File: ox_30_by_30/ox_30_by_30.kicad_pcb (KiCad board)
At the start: 2 copper layers, 30 x 30 mm, 22 parts, among them J1 PIX1, J10 R_CONN, J11 PIX1, J12 PIX2, J13 PIX3, J14 BOT_TCE, J16 PIX4, J17 PIX5, J18 PIX6, J19 TCE4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

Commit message: purge output files
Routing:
- added copper zone on B.Cu, net (none)
- added copper zone on F.Cu, net (none)
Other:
- board text added: "de7ba9e"
- board text removed: "45f1e60"
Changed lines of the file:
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@@
   )
   (setup
-    (last_trace_width 1)
+    (last_trace_width 0.25)
     (user_trace_width 1)
     (trace_clearance 0.2)
-    (zone_clearance 0.508)
+    (zone_clearance 0.2)
     (zone_45_only no)
     (trace_min 0.2)
@@
   (gr_arc (start -8 10) (end -10 10) (angle -90) (layer Edge.Cuts) (width 0.05))
   (gr_arc (start -8 -10) (end -8 -12) (angle -90) (layer Edge.Cuts) (width 0.05))
-  (gr_text 45f1e60 (at 11.5 14) (layer B.SilkS)
+  (gr_text de7ba9e (at 11.5 14) (layer B.SilkS)
     (effects (font (size 1 1) (thickness 0.15)) (justify mirror))
   )
-  (gr_text 45f1e60 (at 11.5 14) (layer F.SilkS)
+  (gr_text de7ba9e (at 11.5 14) (layer F.SilkS)
     (effects (font (size 1 1) (thickness 0.15)))
   )
@@
   (segment (start -12.16 11) (end -11.75 11.41) (width 1) (layer F.Cu) (net 20))
   (segment (start -14 11) (end -12.16 11) (width 1) (layer F.Cu) (net 20))
+  (zone (net 0) (net_name "") (layer F.Cu) (hatch edge 0.508)
+    (connect_pads (clearance 0.2))
+    (min_thickness 0.1)
+    (fill yes (arc_segments 32) (thermal_gap 0.508) (thermal_bridge_width 0.508))
+    (polygon
+      (pts
+        (xy 14.5 14.5) (xy -14.5 14.5) (xy -14.5 -14.5) (xy 14.5 -14.5)
+      )
+    )
+  )
+  (zone (net 0) (net_name "") (layer B.Cu) (hatch edge 0.508)
+    (connect_pads (clearance 0.2))
+    (min_thickness 0.1)
+    (fill yes (arc_segments 32) (thermal_gap 0.508) (thermal_bridge_width 0.508))
+    (polygon
+      (pts
+        (xy 14.5 14.5) (xy -14.5 14.5) (xy -14.5 -14.5) (xy 14.5 -14.5)
+      )
+    )
+  )
 )

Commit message: update silk
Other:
- board text added: "c0adfdf"
- board text removed: "de7ba9e"
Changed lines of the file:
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@@
   (gr_arc (start -8 10) (end -10 10) (angle -90) (layer Edge.Cuts) (width 0.05))
   (gr_arc (start -8 -10) (end -8 -12) (angle -90) (layer Edge.Cuts) (width 0.05))
-  (gr_text de7ba9e (at 11.5 14) (layer B.SilkS)
+  (gr_text c0adfdf (at 11.5 14) (layer B.SilkS)
     (effects (font (size 1 1) (thickness 0.15)) (justify mirror))
   )
-  (gr_text de7ba9e (at 11.5 14) (layer F.SilkS)
+  (gr_text c0adfdf (at 11.5 14) (layer F.SilkS)
     (effects (font (size 1 1) (thickness 0.15)))
   )

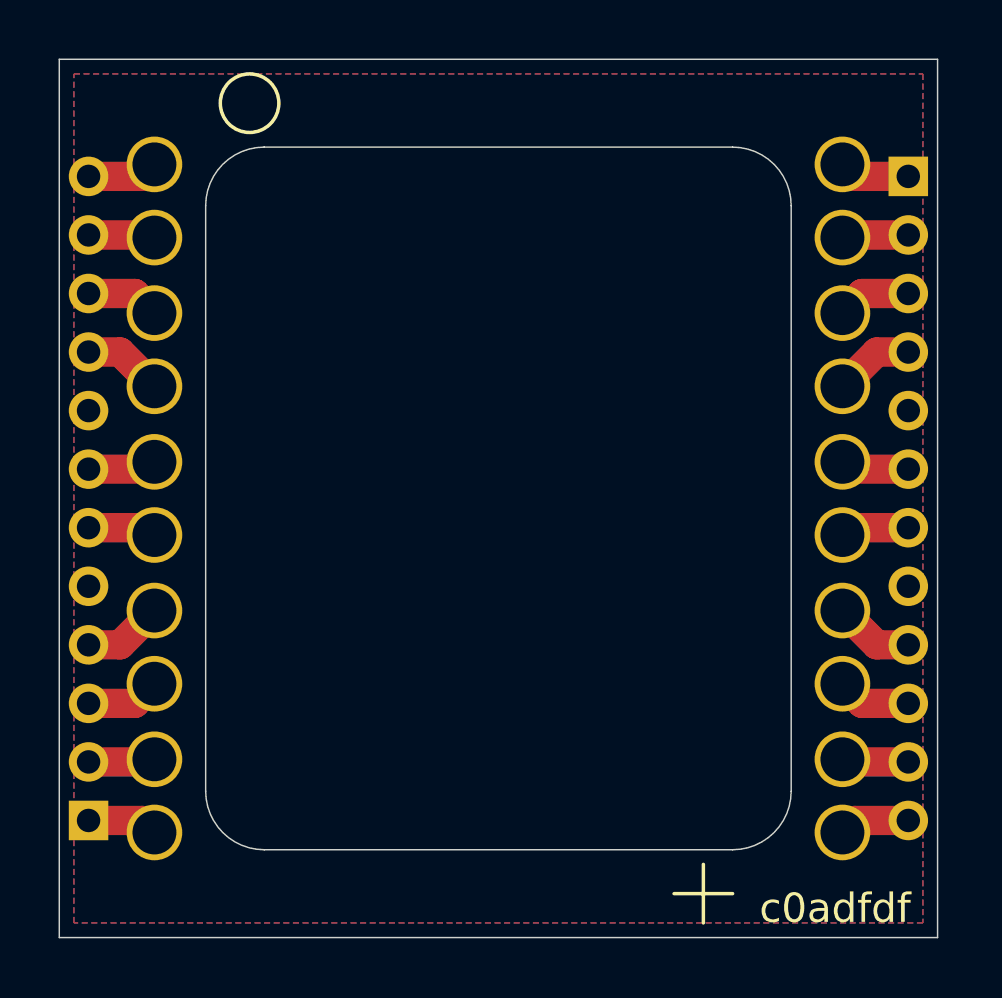
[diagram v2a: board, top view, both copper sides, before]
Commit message: lim crossbar pcb done
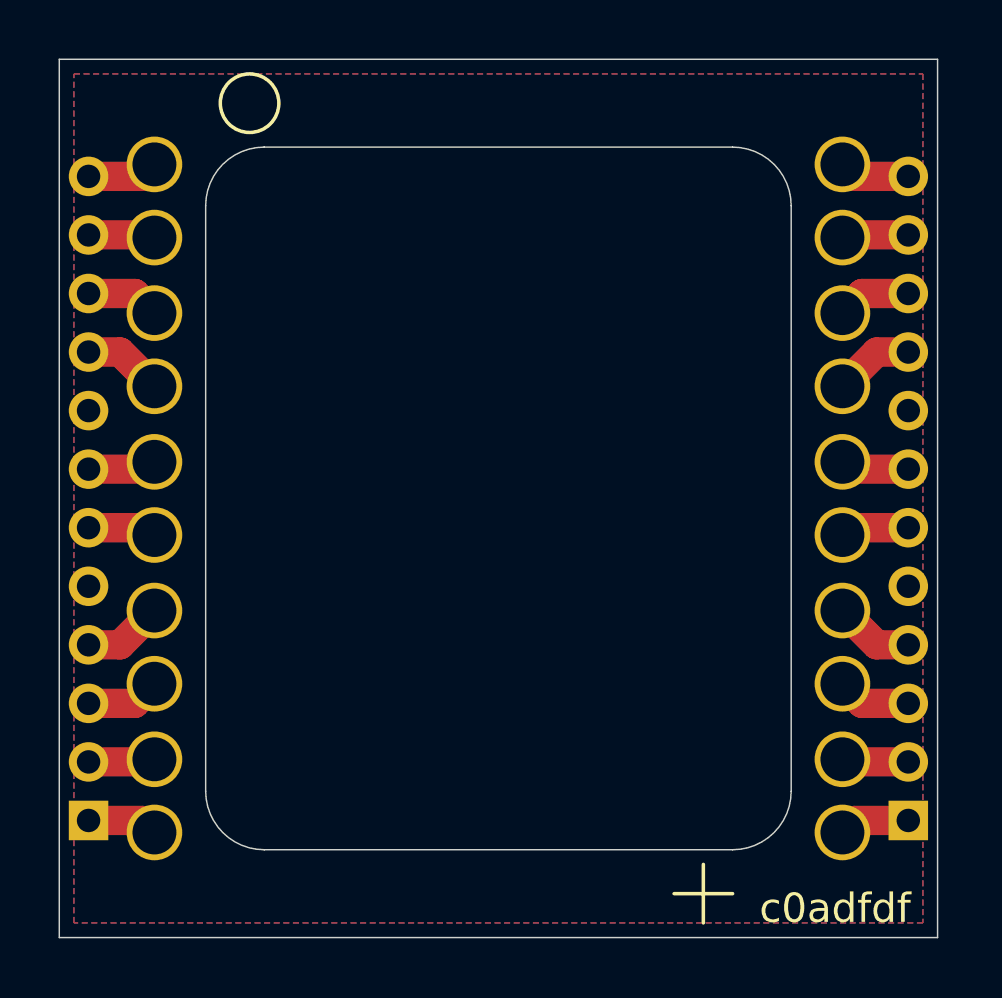
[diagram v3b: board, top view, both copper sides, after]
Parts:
- moved J10 22.0 mm to (14.0, 11.0), turned to 0 degrees
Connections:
- J10 pad 10: Net-(J1-Pad1) -> Net-(J10-Pad10)
- J10 pad 3: Net-(J10-Pad3) -> Net-(J1-Pad1)
- J11 pad 1: Net-(J10-Pad9) -> Net-(J10-Pad4)
- J13 pad 1: Net-(J10-Pad6) -> Net-(J10-Pad7)
- J14 pad 1: Net-(J10-Pad11) -> Net-(J10-Pad2)
- J17 pad 1: Net-(J10-Pad4) -> Net-(J10-Pad9)
- J23 pad 1: Net-(J10-Pad1) -> Net-(J10-Pad12)
- J24 pad 1: Net-(J10-Pad2) -> Net-(J10-Pad11)
- J3 pad 1: Net-(J10-Pad7) -> Net-(J10-Pad6)
- J5 pad 1: Net-(J10-Pad3) -> Net-(J10-Pad10)
- J9 pad 1: Net-(J10-Pad12) -> Net-(J10-Pad1)
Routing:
- net Net-(J10-Pad3): track 2.53 -> 0.00 mm
- net Net-(J10-Pad10): track 0.00 -> 2.53 mm

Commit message: update spring pin hole size and improve crossbar routing
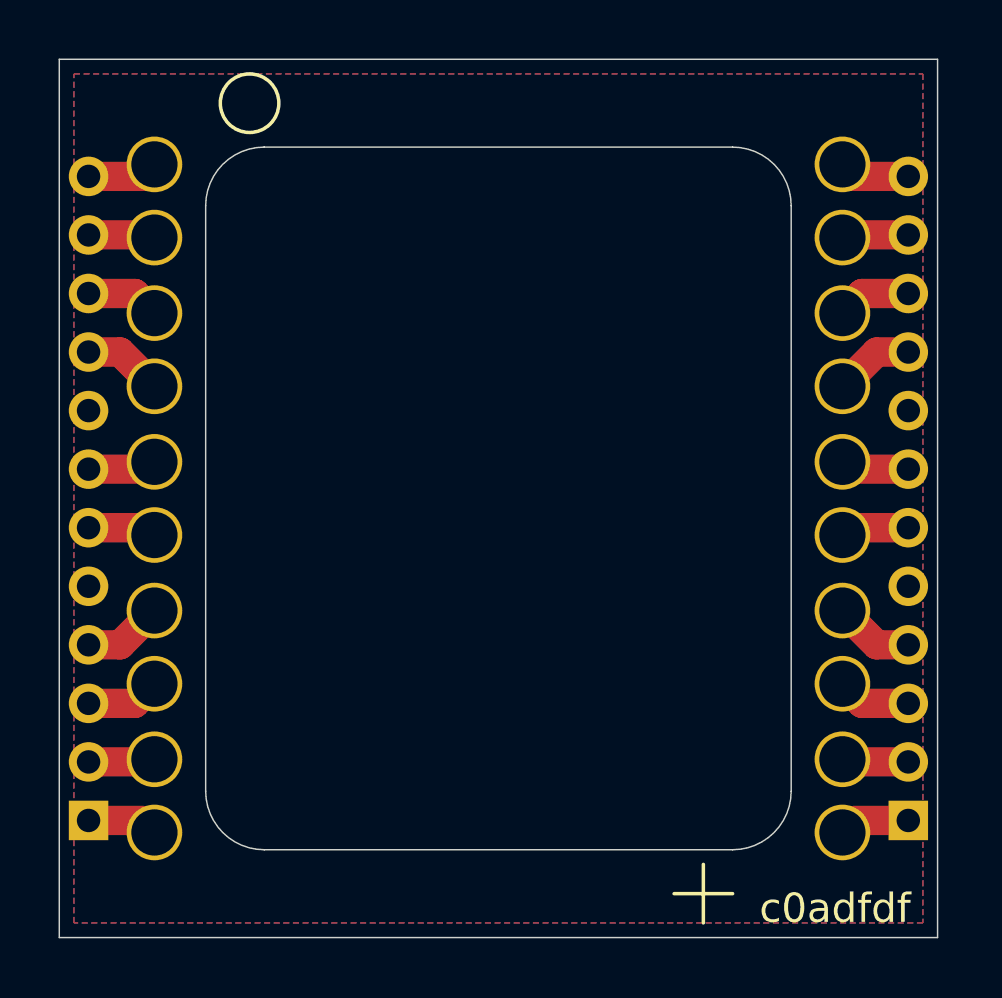
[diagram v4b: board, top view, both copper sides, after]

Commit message: update silk
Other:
- board text added: "365180b"
- board text removed: "c0adfdf"
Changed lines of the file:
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@@
   (gr_arc (start -8 10) (end -10 10) (angle -90) (layer Edge.Cuts) (width 0.05))
   (gr_arc (start -8 -10) (end -8 -12) (angle -90) (layer Edge.Cuts) (width 0.05))
-  (gr_text c0adfdf (at 11.5 14) (layer B.SilkS)
+  (gr_text 365180b (at 11.5 14) (layer B.SilkS)
     (effects (font (size 1 1) (thickness 0.15)) (justify mirror))
   )
-  (gr_text c0adfdf (at 11.5 14) (layer F.SilkS)
+  (gr_text 365180b (at 11.5 14) (layer F.SilkS)
     (effects (font (size 1 1) (thickness 0.15)))
   )
